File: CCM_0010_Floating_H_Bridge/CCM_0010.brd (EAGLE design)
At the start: 82.5 x 76.2 mm, 60 parts, among them IC1 HIP4081A, IC2 74*1G04, Q1 TIP29, Q2 TIP30, U1 ADA4898-2, U2 AD8276, U3 BUF634, U4 AD4898-1, X1 1-227161-0, X2 22-23-2021, X3 1-227161-0, X4 22-23-2031, X5 22-23-2031, X6 22-23-2031, X7 22-23-2031

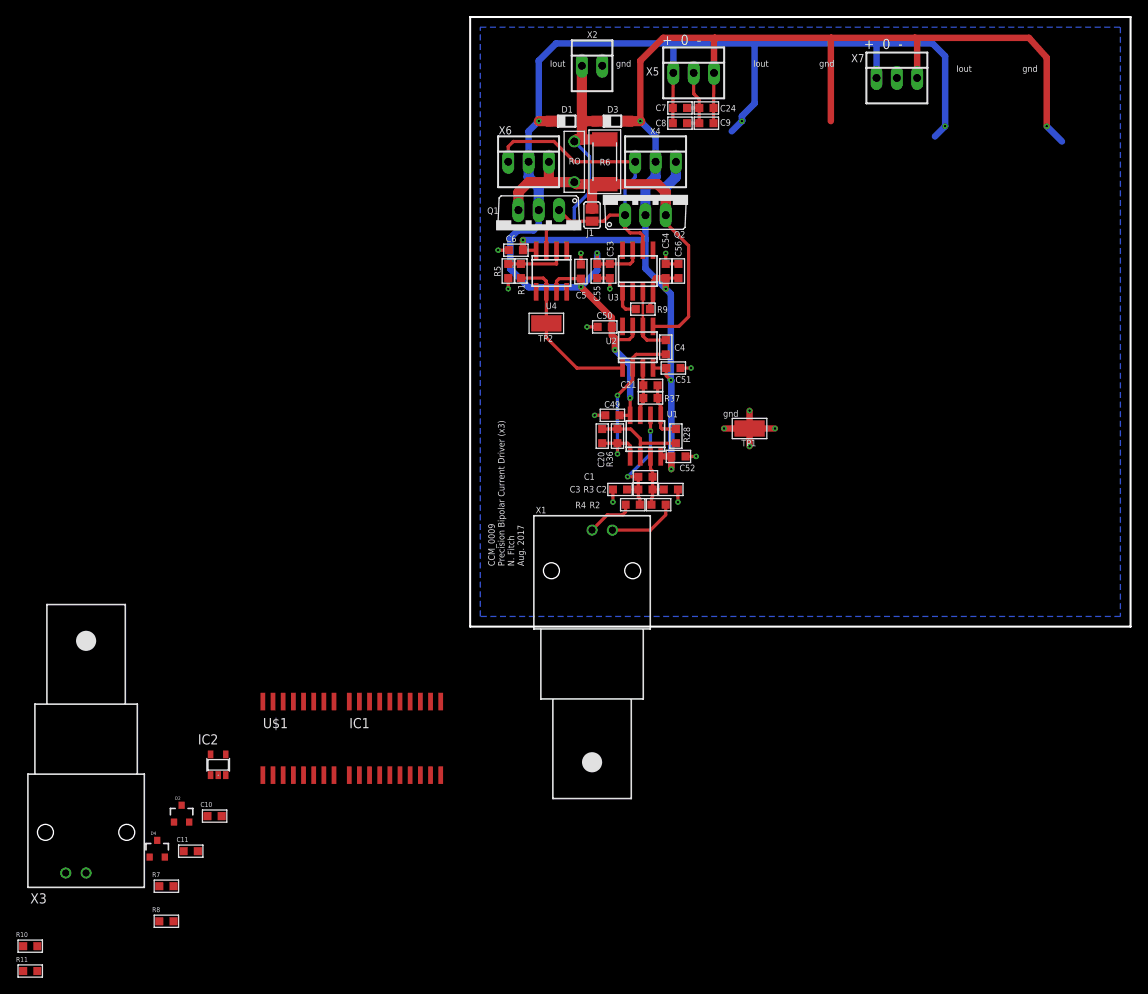
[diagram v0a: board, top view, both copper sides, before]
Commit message: Added production files for CCM_0010
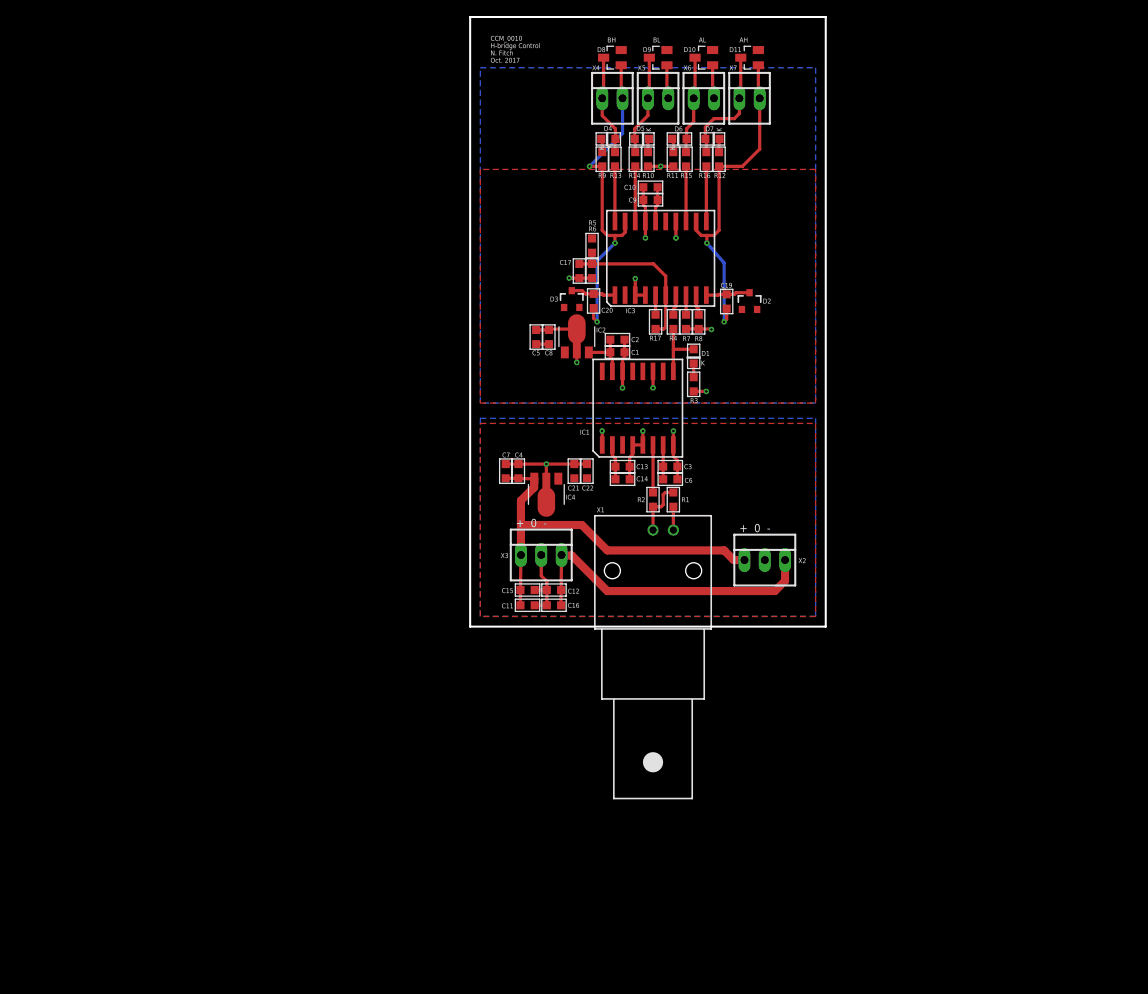
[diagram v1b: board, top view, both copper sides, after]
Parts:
- removed C24, C49, C50, C51, C52, C53, C54: 0.1u, acrooptics:0603
- removed C55, C56: 4.7u, acrooptics:0603
- removed J1: (no value), acrooptics:SJ
- removed Q1: TIP29, transistor-power:TO220AV
- removed Q2: TIP30, transistor-power:TO220AV
- removed R28: DNI, acrooptics:0603
- removed R36, R37: 1.000k, acrooptics:0603
- removed RO: 1.00, noah:LTO30
- removed TP1, TP2: TESTPOINT, Fitch:TESTPOINT
- removed U$1: ADUM5230, noah:SO16W
- removed U1: ADA4898-2, noah:SO8
- removed U2: AD8276, noah:SO8
- removed U3: BUF634, noah:SO8
- removed U4: AD4898-1, noah:SO8
- added C12, C13, C17, C22: 0.1u, acrooptics:0603
- added C14, C15, C16: 4.7u, acrooptics:0603
- added C19: 0.1uF, acrooptics:0603
- added D10, D11, D8, D9: (no value), WCSMain:SOT23
- added D5, D6, D7: (no value), acrooptics:LED0603
- added IC3: HIP4080A, noah:SO20W
- added IC4: 78L05F, linear:SOT89
- added R12: 10k, acrooptics:0603
- added R13, R14, R15, R16: 100, acrooptics:0603
- added R17: 100k, acrooptics:0603
- C1: value 10nF -> 0.1u
- C10, C11: value 47pF -> 0.1u
- C2, C3: value 1nF -> 4.7u
- C20: value 47pF -> 0.1uF
- C21: value 47pF -> 4.7u
- C4: value DNI -> 4.7u
- C7: value 4.7u -> 0.1u
- C8: value 0.1u -> 4.7u
- D1: value BAV19W -> (none); device AquariumLibrary:SOD123 -> acrooptics:LED0603
- D3: value BAV19W -> (none); device AquariumLibrary:SOD123 -> WCSMain:SOT23-3
- D4: device WCSMain:SOT23-3 -> acrooptics:LED0603
- IC1: value HIP4081A -> ADUM5230; device noah:SO20 -> noah:SO16W
- IC2: value 74*1G04 -> 78L12F; device noah:SOT23-5 -> linear:SOT89
- R1: value 10.00k -> 10k
- R10: value 100 -> 10k
- R2, R4: value 1.000k -> 100
- R3: value 1M -> 1k
- R5: value 1.000k -> 10k
- R6: value DNI -> 10k; device noah:2512 -> acrooptics:0603
- R7, R8: value (none) -> 100k
- R9: value DNI -> 10k
- X2: value 22-23-2021 -> 22-23-2031; device con-molex:22-23-2021 -> con-molex:22-23-2031
- X3: value 1-227161-0 -> 22-23-2031; device con-coax:AMP_227161 -> con-molex:22-23-2031
- X4, X5, X6, X7: value 22-23-2031 -> 22-23-2021; device con-molex:22-23-2031 -> con-molex:22-23-2021
- moved R11 129.5 mm to (25.4, 58.4), turned to 270 degrees
- moved R10 125.0 mm to (22.2, 58.4), turned to 270 degrees
- moved D4 105.2 mm to (17.3, 61.0), turned to 90 degrees
- moved R8 100.2 mm to (28.6, 38.1), turned to 90 degrees
- moved R7 95.9 mm to (27.0, 38.1), turned to 90 degrees
- moved C10 95.6 mm to (22.5, 54.9), turned to 180 degrees
- moved D2 95.6 mm to (34.9, 40.6)
- moved IC2 69.8 mm to (13.3, 36.3)
- moved X3 66.6 mm to (8.89, 8.95)
- moved X2 65.4 mm to (36.8, 8.32)
- moved C11 52.1 mm to (7.18, 2.67)
- moved IC1 51.2 mm to (21.0, 27.3)
- moved C7 50.4 mm to (4.45, 19.4), turned to 90 degrees
- moved C6 34.5 mm to (25.0, 18.4), turned to 180 degrees
- moved R1 34.3 mm to (25.4, 15.9), turned to 90 degrees
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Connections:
- removed net N$14: R9.1, U3.1
- removed net N$15: R1.2, TP2.P$1, U2.1, U4.6
- removed net N$26: C20.1, R28.2, R36.2, U1.2
- removed net N$27: IC1.14
- removed net N$31: C21.1, R28.1, R37.2, U1.5
- removed net N$33: C21.2, R37.1, U1.7, U2.3
- removed net N$35: C20.2, C4.1, R36.1, U1.1, U2.2
- new net N$24: IC3.8, R7.2
- net +12V: now also C10.1, C5.1, C8.1, C9.1, D3.1, IC1.10, IC2.1, IC3.15, IC3.16, IC3.2, R5.1; no longer D4.1, IC1.15, IC1.16, IC1.2, IC1.7, U$1.10, U$1.15
- net +5V: now also C13.1, C14.1, C21.1, C22.1, C3.2, C6.2, IC1.2, IC1.7, IC4.1; no longer IC2.5, U$1.2, U$1.7
- net AGND: now also C1.2, C10.2, C17.2, C2.2, C5.2, C8.2, C9.2, D10.1, D9.1, IC1.11, IC1.14, IC2.2, IC2.2@1, IC3.14, IC3.17, IC3.3, IC3.4, R10.2, R11.2, R3.2, R6.2, X5.2, X6.2; no longer IC1.4, U$1.11, U$1.14
- net GND: now also C11.2, C12.1, C13.2, C14.2, C15.2, C16.1, C21.2, C22.2, C3.1, C4.2, IC1.1, IC1.4, IC1.5, IC1.8, IC4.2, IC4.2@1, R1.1, X1.2; no longer C2.1, C24.1, C3.2, C49.2, C5.2, C50.2, C51.1, C52.1, C53.2, C54.1, C55.2, C56.1, C8.2, C9.1, IC2.3, R11.1, R5.2, TP1.P$1, U$1.1, U$1.4, U$1.8, X5.2, X7.2
- net N$1: now also D1.C, R3.1; no longer R2.1, X1.2
- net N$10: now also C1.1, C2.1, IC1.15, IC2.3; no longer IC2.2, R10.2, U$1.5
- net N$11: now also IC3.11, R16.1; no longer D1.A, D3.C, R6.2, RO.P$2, U4.3, X2.1
- net N$12: now also IC3.13, R15.1; no longer J1.2, Q1.E, Q2.E, R6.1, RO.P$1, U2.5, X4.3, X6.3
- net N$13: now also IC3.7, R4.2; no longer IC1.6, U$1.16
- net N$16: now also IC3.9, R8.2; no longer IC1.5, U$1.9
- net N$17: now also C20.2, D3.3, IC3.1; no longer C10.2, D2.3, IC1.1
- net N$18: now also C20.1, D8.1, IC3.19, R9.2, X4.2; no longer C10.1, IC1.19
- net N$19: now also IC3.18, R14.1; no longer IC1.18
- net N$2: now also D4.C, R9.1; no longer R4.1, X1.1
- net N$20: now also IC3.5, R17.2; no longer IC1.17
- net N$21: now also C19.1, D11.1, IC3.12, R12.2, X7.2; no longer C11.1, IC1.12
- net N$22: now also D11.3, D7.A, R16.2, X7.1; no longer IC1.11
- net N$23: now also C19.2, D2.3, IC3.10; no longer C11.2, D4.3, IC1.10
- net N$25: now also D10.3, D6.A, R15.2, X6.1; no longer IC1.13
- net N$28: now also R1.2, R2.1, X1.1; no longer R10.1, R11.2, X3.1
- net N$29: now also C17.1, IC3.6, R17.1, R5.2, R6.1; no longer IC1.8, R7.2
- net N$3: now also D5.C, R10.1; no longer C4.2, U2.6, U3.3
- net N$30: now also IC1.6, R2.2; no longer IC1.9, R8.2
- net N$4: now also IC3.20, R13.1; no longer IC1.20
- net N$5: now also D5.A, D9.3, R14.2, X5.1; no longer C1.1, C2.2, R2.2, R3.1, U1.3
- net N$6: now also D6.C, R11.1; no longer C1.2, C3.1, R3.2, R4.2, U1.6
- net N$7: now also D4.A, D8.3, R13.2, X4.1; no longer R1.1, R5.1, U4.2
- net N$8: now also D1.A, IC1.9, R4.1; no longer IC2.4, U$1.6
- net N$9: now also D7.C, R12.1; no longer J1.1, Q1.B, Q2.B, U3.6, X4.1, X6.1
- net V+: now also C11.1, C15.1, C4.1, IC4.3, X2.1, X3.1; no longer C49.1, C5.1, C50.1, C53.1, C55.1, C8.1, D1.C, Q1.C, U1.8, U2.7, U3.7, U4.7, X5.1, X6.2, X7.1
- net V-: now also C12.2, C16.2, X2.3, X3.3; no longer C24.2, C51.2, C52.2, C54.2, C56.2, C6.2, C9.2, D3.A, Q2.C, R9.2, U1.4, U2.4, U3.4, U4.4, X4.2, X5.3, X7.3
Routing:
- net V-: track 179.1 -> 39.2 mm, vias 6 -> 0
- net V+: track 172.8 -> 49.9 mm, vias 7 -> 0
- net N$12: track 56.3 -> 6.89 mm
- net AGND: track 0.00 -> 48.6 mm, vias 0 -> 10
- net N$21: track 0.00 -> 42.4 mm, vias 0 -> 2
- net N$18: track 0.00 -> 42.3 mm, vias 0 -> 3
- net N$9: track 41.5 -> 1.68 mm
- net N$11: track 33.5 -> 6.89 mm, vias 1 -> 0
- net N$35: track 23.5 -> 0.00 mm, vias 2 -> 0
- net N$15: track 21.5 -> 0.00 mm
- net N$29: track 0.00 -> 20.5 mm
- net N$22: track 0.00 -> 15.2 mm
- net N$6: track 15.2 -> 1.70 mm, vias 2 -> 0
- net N$25: track 0.00 -> 12.3 mm
- net N$26: track 12.0 -> 0.00 mm
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- added copper zone on layer 1, net +12V
- added copper zone on layer 1, net +5V
- added copper zone on layer 16, net AGND
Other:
- board size 82.5 x 76.2 mm -> 44.5 x 76.2 mm
- board text added: "AH"
- board text added: "AL"
- board text added: "BH"
- board text added: "BL"
- board text added: "CCM_0010 H-bridge Control N. Fitch Oct. 2017"
- board text removed: "CCM_0009 Precision Bipolar Current Driver (x3) N. Fitch Aug. 2017"
- board text removed: "Iout"
- board text removed: "gnd"

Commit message: CCM_0010: component value updates
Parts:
- R3: value 1k -> 10k
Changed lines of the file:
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@@
 <attribute name="VALUE" x="26.797" y="33.782" size="0.6096" layer="27" font="vector" ratio="20" rot="R180"/>
 </element>
-<element name="R3" library="acrooptics" package="0603" value="1k" x="27.94" y="30.2895" smashed="yes" rot="R270">
+<element name="R3" library="acrooptics" package="0603" value="10k" x="27.94" y="30.2895" smashed="yes" rot="R270">
 <attribute name="NAME" x="27.4955" y="27.94" size="0.6096" layer="25" font="vector" ratio="15"/>
 <attribute name="VALUE" x="26.162" y="31.9405" size="0.6096" layer="27" font="vector" ratio="20" rot="R270"/>

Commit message: started design of hardware TCL
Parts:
- R10, R11, R12, R3, R9: value 10k -> 51k
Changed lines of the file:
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@@
 <attribute name="VALUE" x="26.797" y="33.782" size="0.6096" layer="27" font="vector" ratio="20" rot="R180"/>
 </element>
-<element name="R3" library="acrooptics" package="0603" value="10k" x="27.94" y="30.2895" smashed="yes" rot="R270">
+<element name="R3" library="acrooptics" package="0603" value="51k" x="27.94" y="30.2895" smashed="yes" rot="R270">
 <attribute name="NAME" x="27.4955" y="27.94" size="0.6096" layer="25" font="vector" ratio="15"/>
 <attribute name="VALUE" x="26.162" y="31.9405" size="0.6096" layer="27" font="vector" ratio="20" rot="R270"/>
@@
 <attribute name="VALUE" x="17.272" y="62.103" size="0.6096" layer="27" font="vector" ratio="20" rot="R90"/>
 </element>
-<element name="R9" library="acrooptics" package="0603" value="10k" x="16.51" y="58.42" smashed="yes" rot="R270">
+<element name="R9" library="acrooptics" package="0603" value="51k" x="16.51" y="58.42" smashed="yes" rot="R270">
 <attribute name="NAME" x="16.002" y="56.0705" size="0.6096" layer="25" font="vector" ratio="15"/>
 <attribute name="VALUE" x="14.732" y="60.071" size="0.6096" layer="27" font="vector" ratio="20" rot="R270"/>
@@
 <attribute name="VALUE" x="21.463" y="59.817" size="0.6096" layer="27" font="vector" ratio="20" rot="R270"/>
 </element>
-<element name="R10" library="acrooptics" package="0603" value="10k" x="22.225" y="58.42" smashed="yes" rot="R270">
+<element name="R10" library="acrooptics" package="0603" value="51k" x="22.225" y="58.42" smashed="yes" rot="R270">
 <attribute name="NAME" x="21.5265" y="56.0705" size="0.6096" layer="25" font="vector" ratio="15"/>
 <attribute name="VALUE" x="20.447" y="60.071" size="0.6096" layer="27" font="vector" ratio="20" rot="R270"/>
@@
 <attribute name="VALUE" x="26.162" y="62.103" size="0.6096" layer="27" font="vector" ratio="20" rot="R90"/>
 </element>
-<element name="R11" library="acrooptics" package="0603" value="10k" x="25.4" y="58.42" smashed="yes" rot="R270">
+<element name="R11" library="acrooptics" package="0603" value="51k" x="25.4" y="58.42" smashed="yes" rot="R270">
 <attribute name="NAME" x="24.5745" y="56.0705" size="0.6096" layer="25" font="vector" ratio="15"/>
 <attribute name="VALUE" x="23.622" y="60.071" size="0.6096" layer="27" font="vector" ratio="20" rot="R270"/>
@@
 <attribute name="VALUE" x="30.2895" y="59.817" size="0.6096" layer="27" font="vector" ratio="20" rot="R270"/>
 </element>
-<element name="R12" library="acrooptics" package="0603" value="10k" x="31.115" y="58.42" smashed="yes" rot="R270">
+<element name="R12" library="acrooptics" package="0603" value="51k" x="31.115" y="58.42" smashed="yes" rot="R270">
 <attribute name="NAME" x="30.48" y="56.0705" size="0.6096" layer="25" font="vector" ratio="15"/>
 <attribute name="VALUE" x="29.337" y="60.071" size="0.6096" layer="27" font="vector" ratio="20" rot="R270"/>
